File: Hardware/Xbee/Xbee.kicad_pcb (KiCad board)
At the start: 2 copper layers, 100 x 50 mm, 48 parts, among them J1 Alimentación, J2 Raspberry, J3 Pines 1, J4 Pines 2, J5 Programación, J6 Entrada, J7 Salida, J8 Batería, K1 SANYOU_SRD_Form_C, Q1 2N7002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

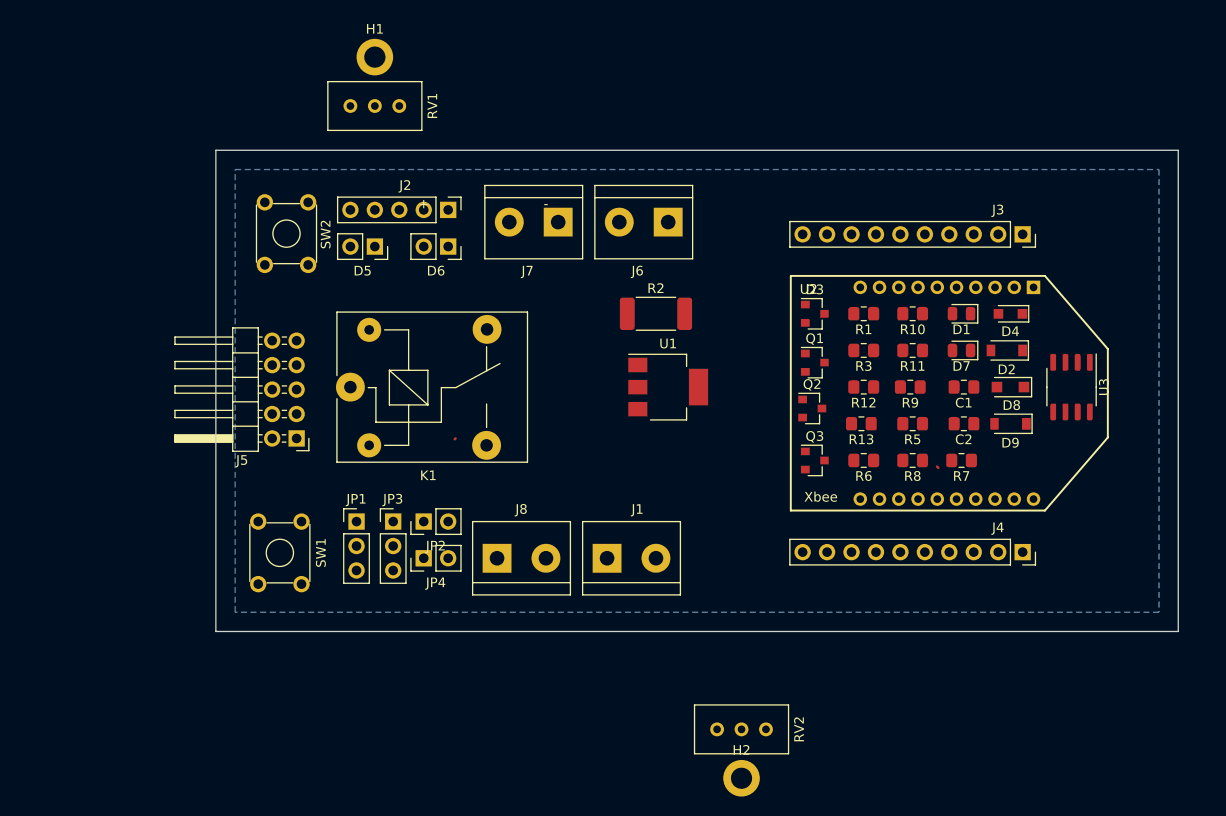
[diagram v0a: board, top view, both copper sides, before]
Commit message: PCB Component placement
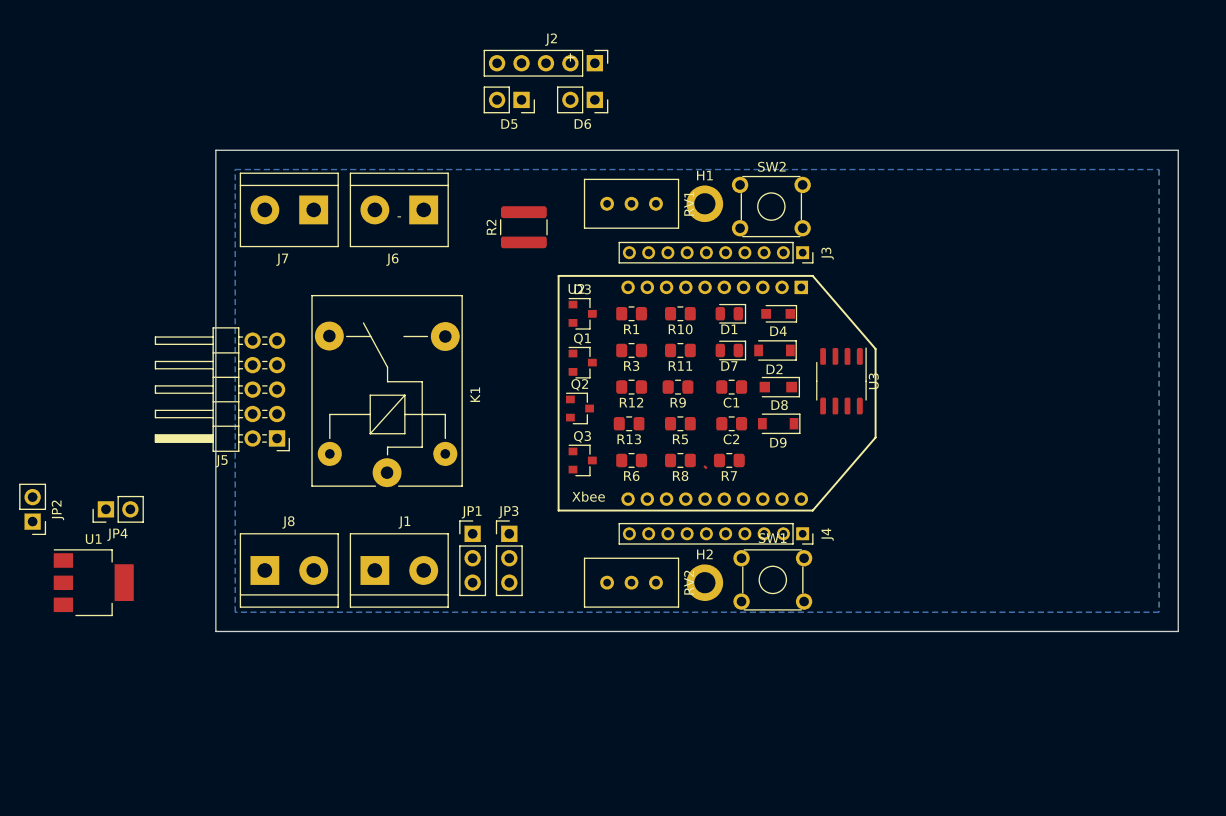
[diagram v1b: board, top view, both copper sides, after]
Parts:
- J3, J4: footprint Connector_PinSocket_2.54mm:PinSocket_1x10_P2.54mm_Vertical -> Connector_PinSocket_2.00mm:PinSocket_1x10_P2.00mm_Vertical
- R2: footprint Resistor_SMD:R_2512_6332Metric_Pad1.52x3.35mm_HandSolder -> Resistor_SMD:R_1218_3246Metric_Pad1.22x4.75mm_HandSolder
- moved U1 63.1 mm to (67.3, 74.9)
- moved SW2 56.0 mm to (141.0, 38.1), turned to 180 degrees
- moved SW1 45.9 mm to (134.6, 72.4), turned to 0 degrees
- moved JP2 40.6 mm to (61.0, 68.6), turned to 180 degrees
- moved H1 37.5 mm to (130.8, 35.6)
- moved JP4 33.4 mm to (68.6, 67.3)
- moved RV1 28.5 mm to (125.7, 35.6)
- moved J6 25.4 mm to (101.6, 36.2)
- moved J7 25.4 mm to (90.2, 36.2)
- moved J1 24.2 mm to (96.5, 73.7)
- moved J8 24.2 mm to (85.1, 73.7)
- moved D3 24.1 mm to (118.1, 47.0)
- moved Q1 24.1 mm to (118.1, 52.1)
- moved Q3 24.1 mm to (118.1, 62.2)
- moved C1 24.1 mm to (133.6, 54.6)
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
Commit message: Add Fuse
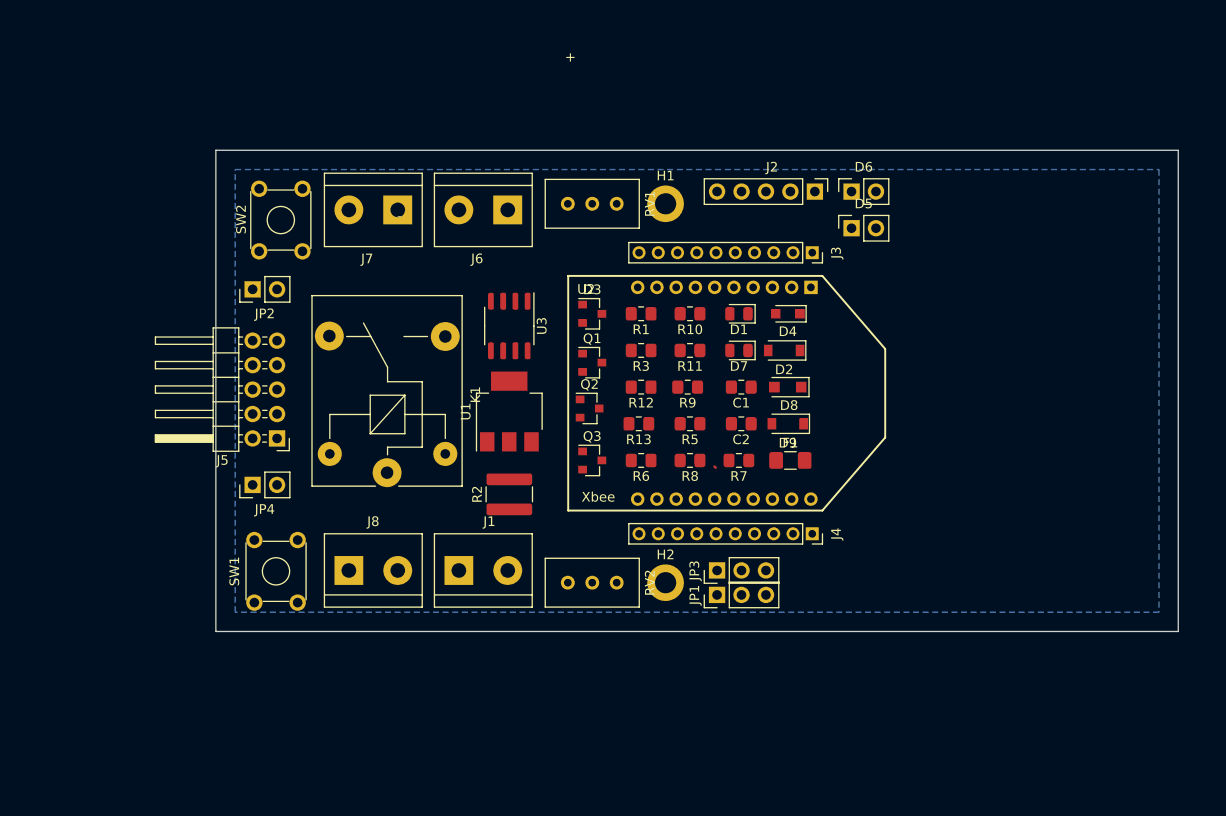
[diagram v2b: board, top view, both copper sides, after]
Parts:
- added F1: Fuse_Small, Fuse:Fuse_1206_3216Metric_Pad1.42x1.75mm_HandSolder, F.Cu at (139.7, 62.2)
- moved SW2 52.1 mm to (89.0, 34.0), turned to 270 degrees
- moved SW1 50.8 mm to (84.0, 77.0), turned to 90 degrees
- moved U1 46.7 mm to (110.5, 57.1), turned to 90 degrees
- moved D5 36.8 mm to (146.1, 38.1), turned to 90 degrees
- moved U3 35.0 mm to (110.5, 48.3)
- moved JP2 33.2 mm to (83.8, 44.5), turned to 90 degrees
- moved D6 28.3 mm to (146.1, 34.3), turned to 90 degrees
- moved R2 27.8 mm to (110.5, 65.7)
- moved J2 26.5 mm to (142.2, 34.3)
- moved JP1 26.2 mm to (132.1, 76.2), turned to 90 degrees
- moved JP3 21.9 mm to (132.1, 73.7), turned to 90 degrees
- moved JP4 15.5 mm to (83.8, 64.8)
- moved J1 8.73 mm to (105.2, 73.7)
- moved J6 8.73 mm to (110.3, 36.2)
- moved J7 8.73 mm to (98.9, 36.2)
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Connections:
- D8 pad 1: +12V -> Net-(D8-Pad1)
- D9 pad 1: +12V -> Net-(D8-Pad1)
- SW1 pad 2: /RST -> GNDREF
- SW1 pad 3: GNDREF -> /RST
- SW2 pad 2: /Comm. -> GNDREF
- SW2 pad 3: GNDREF -> /Comm.

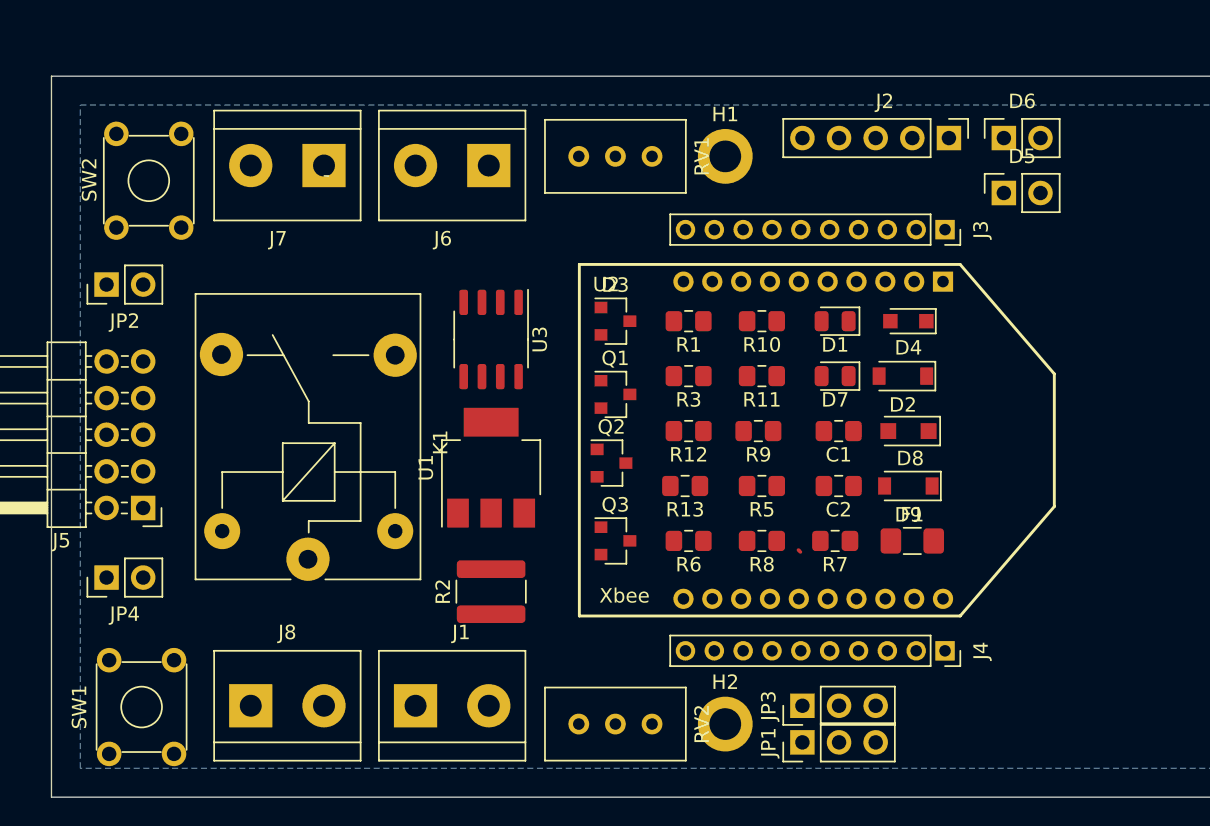
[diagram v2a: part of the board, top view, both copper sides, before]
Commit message: Localización de componentes
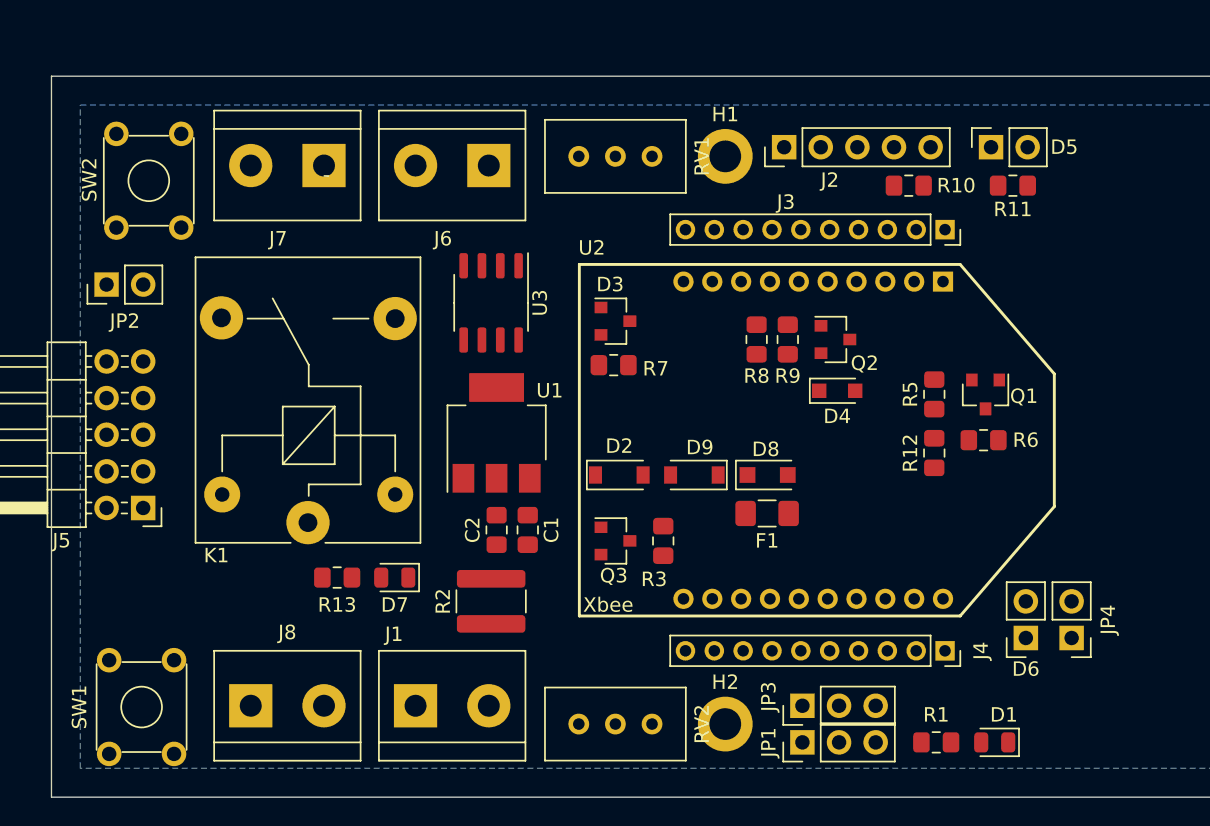
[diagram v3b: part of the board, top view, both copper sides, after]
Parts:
- moved JP4 67.1 mm to (150.7, 69.0), turned to 180 degrees
- moved D6 34.7 mm to (147.6, 69.0), turned to 180 degrees
- moved R1 33.9 mm to (141.4, 76.2)
- moved D7 33.6 mm to (103.8, 64.8)
- moved D1 31.2 mm to (145.4, 76.2)
- moved Q1 25.7 mm to (144.8, 52.1), turned to 270 degrees
- moved R13 25.0 mm to (99.8, 64.8), turned to 0 degrees
- moved C2 23.9 mm to (110.9, 61.5), turned to 270 degrees
- moved C1 22.6 mm to (113.0, 61.5), turned to 270 degrees
- moved R11 21.8 mm to (146.7, 37.6)
- moved R6 21.6 mm to (144.6, 55.2), turned to 0 degrees
- moved D2 20.8 mm to (119.4, 57.7), turned to 0 degrees
- moved R7 19.6 mm to (119.0, 50.0)
- moved Q2 17.7 mm to (134.4, 48.3)
- moved R12 17.1 mm to (141.2, 56.1), turned to 90 degrees
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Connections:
- SW1 pad 2: GNDREF -> /RST
- SW1 pad 3: /RST -> GNDREF
- SW2 pad 2: GNDREF -> /Comm.
- SW2 pad 3: /Comm. -> GNDREF

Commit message: Localización 2
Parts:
- added REF**: MountingHole_2.1mm, MountingHole:MountingHole_2.1mm, F.Cu at (78.7, 81.3)
- added REF**: MountingHole_2.1mm, MountingHole:MountingHole_2.1mm, F.Cu at (180.3, 81.3)
- added REF**: MountingHole_2.1mm, MountingHole:MountingHole_2.1mm, F.Cu at (180.3, 30.5)
- added REF**: MountingHole_2.1mm, MountingHole:MountingHole_2.1mm, F.Cu at (78.7, 29.2)
- D4: footprint Diode_SMD:D_SOD-323_HandSoldering -> Diode_SMD:D_SOD-123F
- moved JP2 46.4 mm to (129.5, 36.8), turned to 180 degrees
- moved RV1 42.4 mm to (137.4, 74.9), turned to 90 degrees
- moved H1 39.8 mm to (132.3, 74.9), turned to 180 degrees
- moved D1 37.9 mm to (114.3, 54.6)
- moved J5 37.1 mm to (115.3, 36.8), turned to 90 degrees
- moved JP3 36.9 mm to (115.6, 40.6)
- moved JP4 34.8 mm to (147.3, 34.3), turned to 0 degrees
- moved D6 32.5 mm to (139.7, 37.5), turned to 90 degrees
- moved D4 32.4 mm to (105.4, 66.0), turned to 270 degrees
- moved Q2 32.3 mm to (104.1, 59.7)
- moved R1 29.2 mm to (123.2, 53.3), turned to 0 degrees
- moved F1 28.6 mm to (101.6, 66.0), turned to 90 degrees
- moved R13 27.2 mm to (123.2, 50.8)
- moved U3 24.5 mm to (133.3, 54.6)
- moved R10 24.5 mm to (123.2, 55.9), turned to 0 degrees
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
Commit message: Comienzo de ruteo
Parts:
- moved SW2 74.7 mm to (150.4, 76.4), turned to 90 degrees
- moved SW1 73.7 mm to (148.5, 40.4)
- moved R8 41.5 mm to (100.6, 65.9), turned to 180 degrees
- moved D5 38.8 mm to (162.1, 63.5), turned to 270 degrees
- moved JP4 37.5 mm to (118.4, 58.2), turned to 180 degrees
- moved D6 37.5 mm to (162.2, 67.4), turned to 270 degrees
- moved R13 37.1 mm to (87.9, 39.1), turned to 90 degrees
- moved D7 28.0 mm to (87.9, 35.2), turned to 270 degrees
- moved R9 24.5 mm to (100.6, 67.9), turned to 0 degrees
- moved R3 22.0 mm to (107.3, 56.9), turned to 90 degrees
- moved R1 19.3 mm to (113.0, 69.7), turned to 90 degrees
- moved R12 17.7 mm to (154.1, 67.4), turned to 180 degrees
- moved Q3 17.6 mm to (110.8, 56.9)
- moved J1 17.2 mm to (88.0, 73.3)
- moved D4 16.8 mm to (88.6, 64.9), turned to 0 degrees
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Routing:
- net +12V: track 0.00 -> 60.8 mm
- net /Bat+: track 0.00 -> 38.3 mm
- net /Vin+: track 0.00 -> 28.9 mm, vias 0 -> 1
- net /Bobina: track 0.00 -> 26.5 mm
- net /DIO2-Entrada: track 0.00 -> 25.9 mm
- net /RXD: track 0.00 -> 25.1 mm
- net /RST: track 0.00 -> 24.3 mm
- net /TXD: track 0.00 -> 24.1 mm
- net Net-(D3-Pad1): track 0.00 -> 17.4 mm
- net /Salida-Rele: track 0.00 -> 15.1 mm
- net +3V3: track 0.00 -> 14.3 mm, vias 0 -> 4
- net /Comm.: track 0.00 -> 12.5 mm
- net /LED-Assoc-RSSI: track 0.00 -> 10.5 mm, vias 0 -> 1
- net Net-(D8-Pad1): track 0.00 -> 6.59 mm
- net Net-(D5-Pad2): track 0.00 -> 4.82 mm
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- added copper zone on F.Cu, net +3V3
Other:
- board text removed: "-"

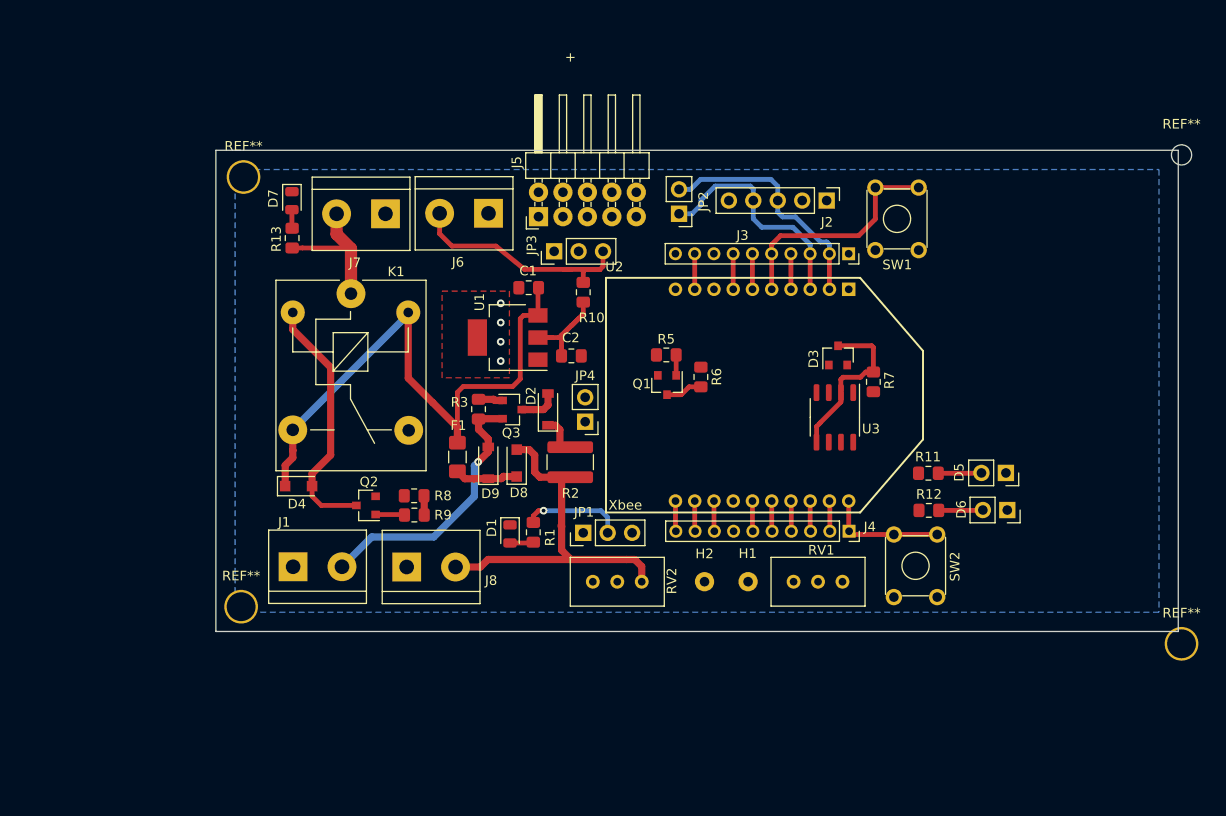
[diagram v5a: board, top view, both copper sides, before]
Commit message: Ruteo, agregado de plano masa
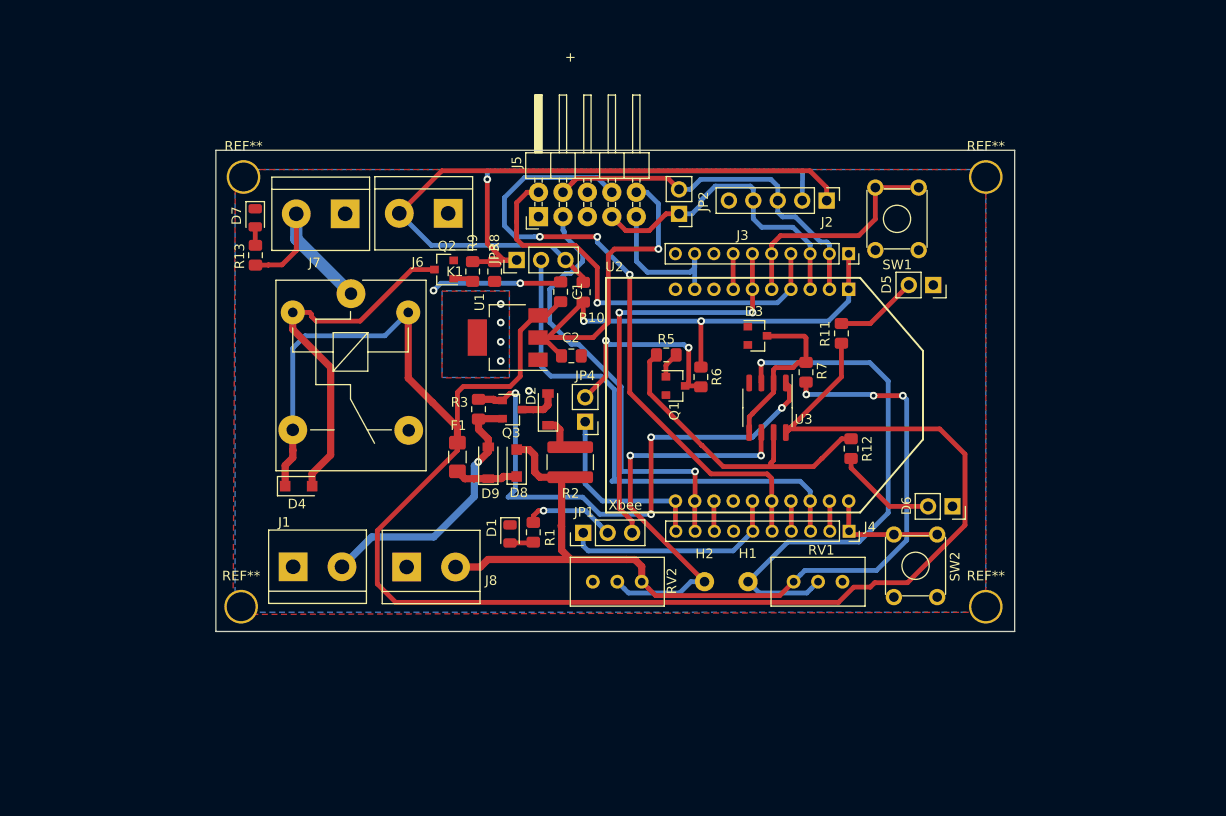
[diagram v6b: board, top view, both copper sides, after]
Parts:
- moved R9 26.0 mm to (106.7, 42.6), turned to 90 degrees
- moved Q2 25.8 mm to (103.7, 42.4)
- moved R8 24.8 mm to (109.0, 42.6), turned to 270 degrees
- moved D5 20.9 mm to (154.5, 44.0)
- moved REF** 20.7 mm to (160.0, 77.4)
- moved REF** 20.5 mm to (160.0, 32.8)
- moved R11 17.1 mm to (145.0, 49.0), turned to 270 degrees
- moved R12 10.3 mm to (146.0, 61.0), turned to 90 degrees
- moved D3 8.62 mm to (136.3, 49.3), turned to 0 degrees
- moved R7 7.07 mm to (141.3, 53.1)
- moved U3 7.07 mm to (137.3, 56.8)
- moved D6 5.71 mm to (156.5, 67.0)
- moved D7 4.20 mm to (84.1, 37.0)
- moved R13 4.20 mm to (84.1, 40.9)
- moved J6 4.19 mm to (104.1, 36.5)
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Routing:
- net +12V: track 60.8 -> 188.5 mm
- net +3V3: track 14.3 -> 81.2 mm, vias 4 -> 7
- net /RTS: track 3.15 -> 67.2 mm, vias 0 -> 3
- net /Bat+: track 38.3 -> 95.4 mm, vias 0 -> 3
- net Net-(H1-Pad1): track 0.00 -> 55.6 mm, vias 0 -> 1
- net /CargaBatería: track 2.87 -> 57.1 mm, vias 0 -> 4
- net /DIO2: track 3.15 -> 54.5 mm
- net /DIO2-Salida: track 2.01 -> 51.8 mm, vias 0 -> 2
- net /DIO2-Entrada: track 25.9 -> 70.7 mm
- net /CTS: track 3.15 -> 46.5 mm, vias 0 -> 1
- net Net-(H2-Pad1): track 0.00 -> 42.3 mm, vias 0 -> 2
- net /DSR-DIO12: track 3.70 -> 44.2 mm, vias 0 -> 1
- net /RSSI: track 3.70 -> 43.4 mm, vias 0 -> 2
- net /EstadoBatería: track 0.00 -> 33.2 mm
- net /Assoc.: track 3.15 -> 23.2 mm
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- added copper zone on B.Cu, net +3V3
- added copper zone on F.Cu, net GNDREF
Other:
- board size 100 x 50 mm -> 83 x 50 mm
